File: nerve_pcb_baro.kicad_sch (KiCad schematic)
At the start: 5 parts, among them U4 BMP390

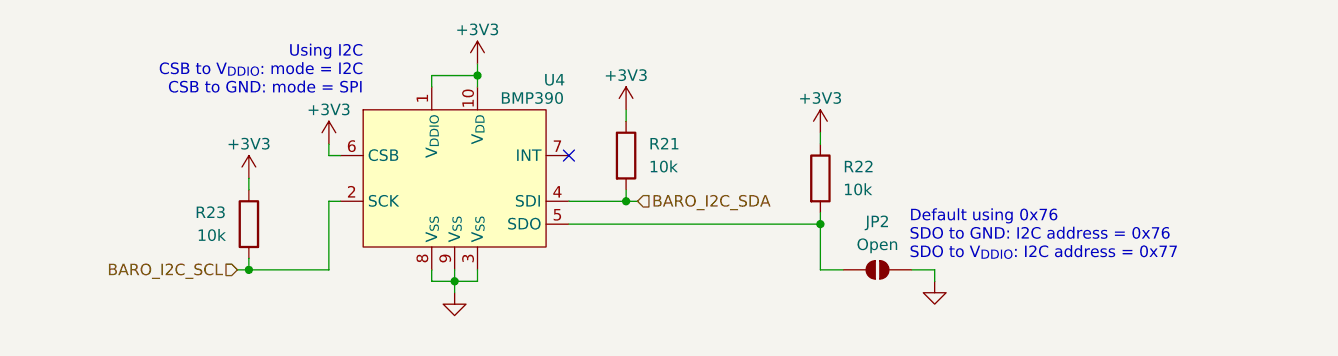
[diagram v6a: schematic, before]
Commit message: Adjust BMP390 address jumper and cleanup PCB
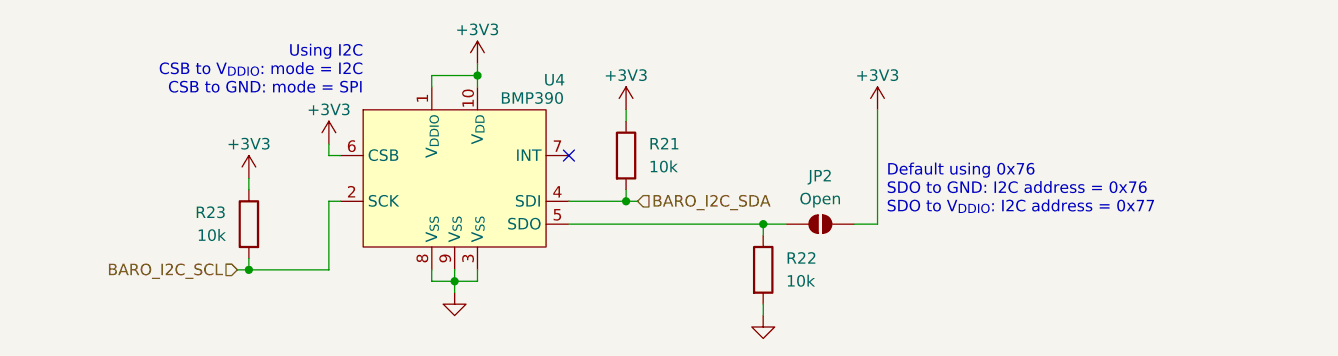
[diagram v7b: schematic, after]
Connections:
- net +3V3: now also JP2.2 (B); no longer R22.1
- net GND: now also R22.2; no longer JP2.2 (B)
- net at JP2.1 (A), U4.5 (SDO): now also R22.1; no longer R22.2

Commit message: Add CAN 120ohm resistors
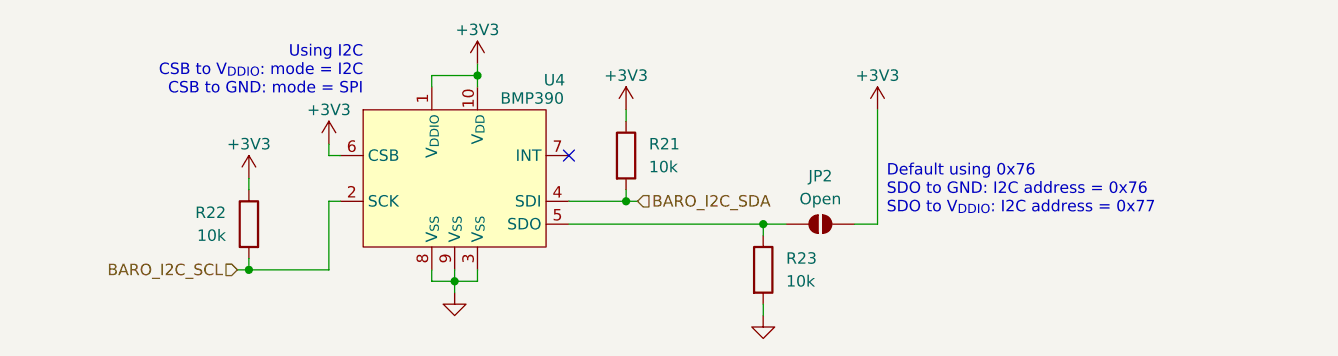
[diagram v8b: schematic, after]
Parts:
- renumbered R23 to R22, R22 to R23
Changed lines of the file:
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@@
 		(dnp no)
 		(fields_autoplaced yes)
-		(property "Reference" "#PWR075"
+		(property "Reference" "#PWR074"
 			(at 137.16 115.57 0)
 			(effects
@@
 			(project "nerve_pcb"
 				(path "/c0277862-b3f2-4e0e-986f-34702f0543f0/9de129d2-0f7b-4a2d-85ad-214e335f6288"
-					(reference "#PWR075")
+					(reference "#PWR074")
 					(unit 1)
 				)
@@
 		(on_board yes)
 		(dnp no)
-		(property "Reference" "R23"
+		(property "Reference" "R22"
 			(at 111.76 100.3299 0)
 			(effects
@@
 			(project "nerve_pcb"
 				(path "/c0277862-b3f2-4e0e-986f-34702f0543f0/9de129d2-0f7b-4a2d-85ad-214e335f6288"
-					(reference "R23")
+					(reference "R22")
 					(unit 1)
 				)
@@
 		(on_board yes)
 		(dnp no)
-		(property "Reference" "R22"
+		(property "Reference" "R23"
 			(at 173.99 105.4099 0)
 			(effects
@@
 			(project "nerve_pcb"
 				(path "/c0277862-b3f2-4e0e-986f-34702f0543f0/9de129d2-0f7b-4a2d-85ad-214e335f6288"
-					(reference "R22")
+					(reference "R23")
 					(unit 1)
 				)
@@
 		(dnp no)
 		(fields_autoplaced yes)
-		(property "Reference" "#PWR074"
+		(property "Reference" "#PWR075"
 			(at 171.45 118.11 0)
 			(effects
@@
 			(project "nerve_pcb"
 				(path "/c0277862-b3f2-4e0e-986f-34702f0543f0/9de129d2-0f7b-4a2d-85ad-214e335f6288"
-					(reference "#PWR074")
-					(unit 1)
-				)
+					(reference "#PWR075")
+					(unit 1)
+				)
